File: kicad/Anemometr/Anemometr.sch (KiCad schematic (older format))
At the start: 154 parts, among them J1 Conn_01x01_Female, J10 Z3, J11 Z3, J12 Z4, J13 Z4, J14 SWD, J15 SWC, J16 Z4, J17 Z4, J18 1, J19 2, J2 Conn_01x01_Female, J20 3, J21 4, J22 5, J23 6, J24 7, J25 8, J26 Z4, J27 Z4, J28 Z4, J29 Z4, J3 RST, J30 Z4, J31 Z4, J32 Z4, J33 Z4, J34 Z4, J35 Z4, J4 TxD, J5 RxD, J6 Z1, J7 Z1, J8 Z2, J9 Z2, U1 TS5A3166DBVR, U10 MCP1700-3002E, U2 LMV7239, U3 TS5A3166DBVR, U4 TS5A3166DBVR, U5 STM32F103C8Tx, U6 TS5A3166DBVR, U7 LM2734Y, U8 MCP1700-5002E, U9 MCP1700-3002E, Y1 8MHz, Y2 25MHz

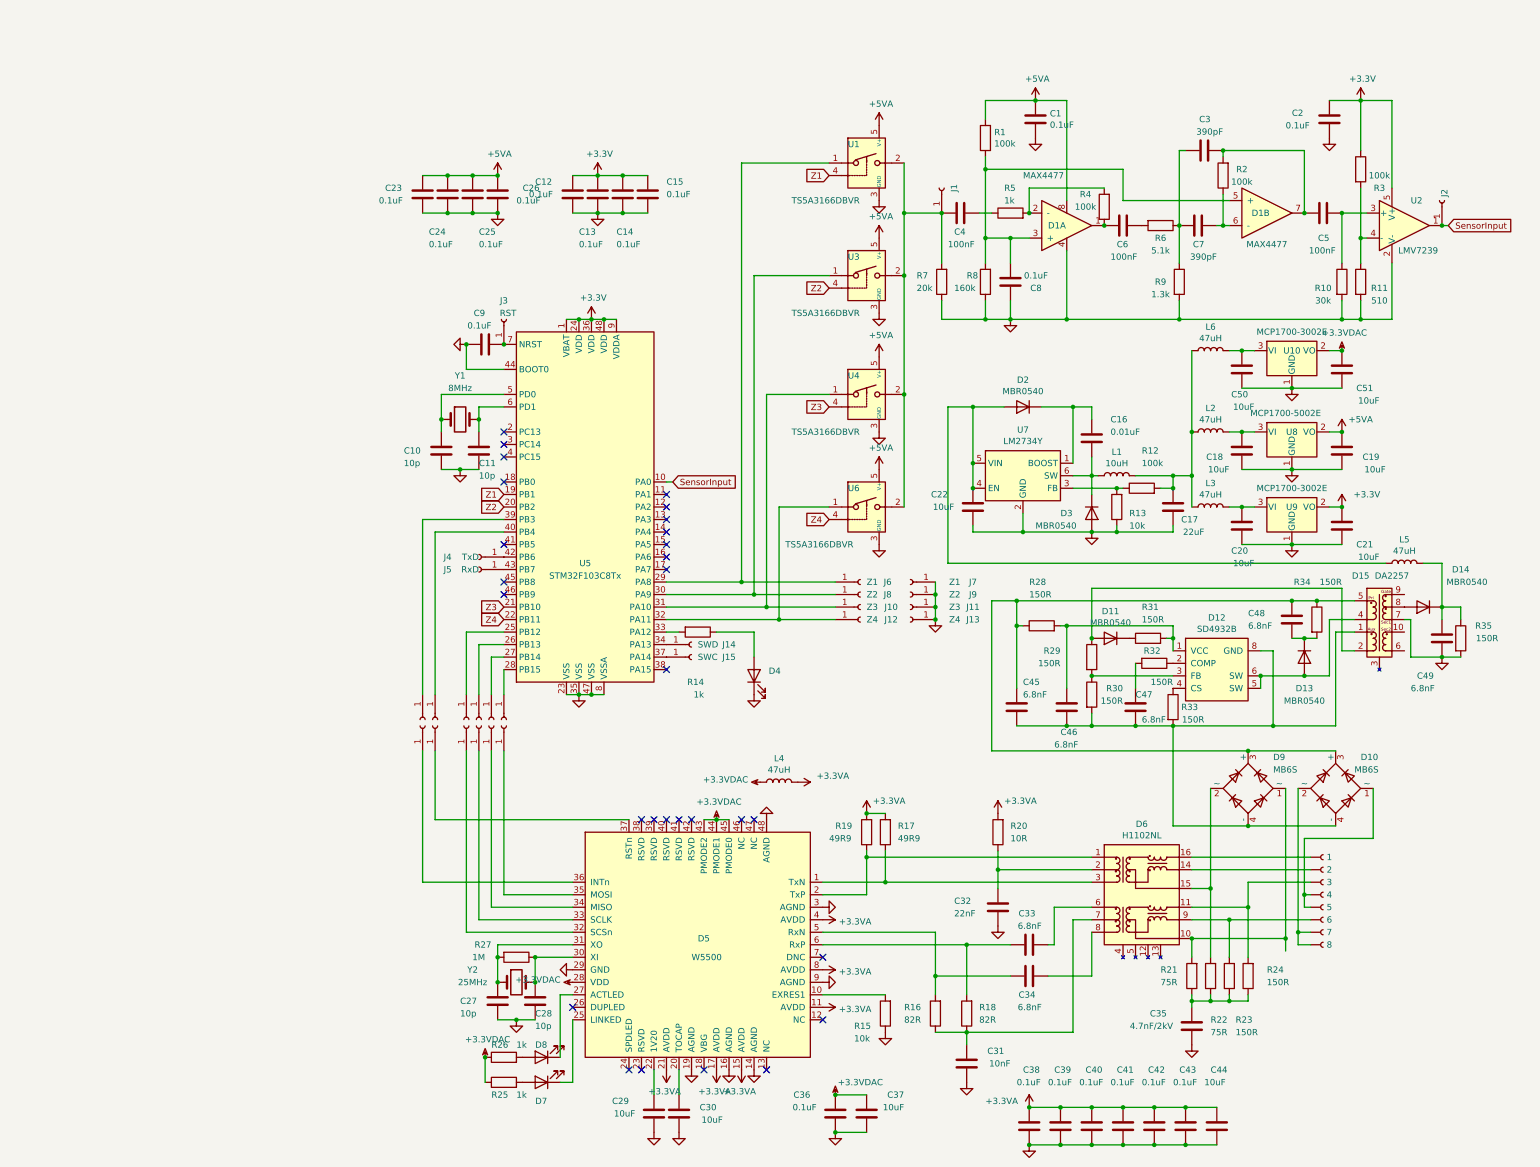
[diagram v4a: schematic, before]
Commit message: изменено:      kicad/Anemometr/Anemometr.kicad_pcb 	изменено:      kicad/Anemometr/Anemometr.kicad_pcb-bak 	изменено:      kicad/Anemometr/Anemometr.sch 	изменено:      kicad/Anemometr/Anemometr.sch-bak
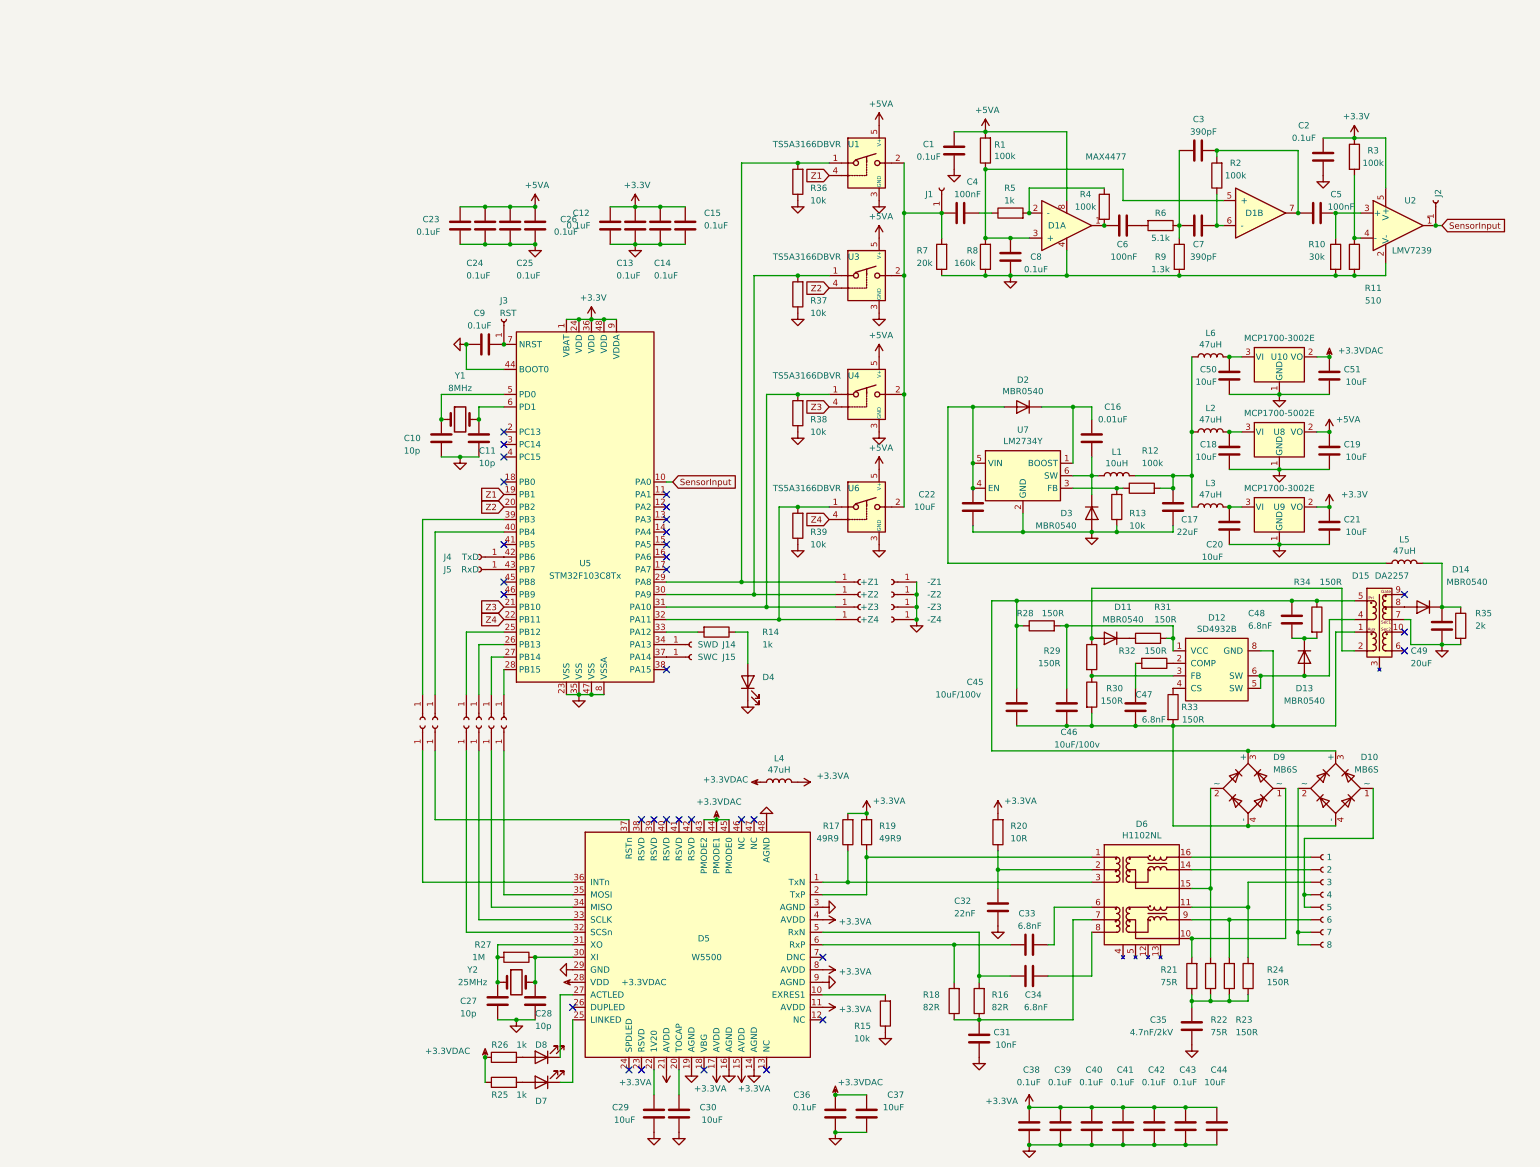
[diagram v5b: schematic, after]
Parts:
- added R36, R37, R38, R39: 10k, Resistor_SMD:R_0805_2012Metric, symbol Device:R
- C45, C46: value 6.8nF -> 10uF/100v
- C49: value 6.8nF -> 20uF
- J10: value Z3 -> +Z3
- J11: value Z3 -> -Z3
- J12: value Z4 -> +Z4
- J13: value Z4 -> -Z4
- J6: value Z1 -> +Z1
- J7: value Z1 -> -Z1
- J8: value Z2 -> +Z2
- J9: value Z2 -> -Z2
- R35: value 150R -> 2k
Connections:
- net GND: now also R36.1, R37.1, R38.1, R39.1
- net at J6.1 (Pin_1), U1.1, U5.29 (PA8): now also R36.2
- net at J8.1 (Pin_1), U3.1, U5.30 (PA9): now also R37.2
- net at J10.1 (Pin_1), U4.1, U5.31 (PA10): now also R38.2
- net at J12.1 (Pin_1), U5.32 (PA11), U6.1: now also R39.2
- no-connect marks 29 -> 32
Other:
- moved on the sheet: C1, C10, C11, C12, C13, C14, C15, C18, C19, C2, C20, C21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

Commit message: изменено:      kicad/Anemometr/Anemometr.sch 	изменено:      kicad/Anemometr/Anemometr.sch-bak 	изменено:      stm32cubeide/Anemometer/Anemometer.ioc 	изменено:      stm32cubeide/Anemometer/Core/Inc/main.h 	изменено:      stm32cubeide/Anemometer/Core/Src/main.c 	изменено:      stm32cubeide/Anemometer/Core/Src/stm32f1xx_it.c 	изменено:      stm32cubeide/Anemometer/Release/Anemometer.bin 	изменено:      stm32cubeide/Anemometer/Release/Anemometer.elf 	изменено:      stm32cubeide/Anemometer/Release/Anemometer.list 	изменено:      stm32cubeide/Anemometer/Release/Anemometer.map 	изменено:      stm32cubeide/Anemometer/Release/Core/Src/main.o 	изменено:      stm32cubeide/Anemometer/Release/Core/Src/main.su 	изменено:      stm32cubeide/Anemometer/Release/Core/Src/stm32f1xx_it.o 	изменено:      stm32cubeide/Anemometer/Release/Core/Src/stm32f1xx_it.su
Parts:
- C5: value 100nF -> 1.5nF
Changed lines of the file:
@@
 P 10950 2100
 F 0 "C5" V 11100 1900 50  0000 L CNN
-F 1 "100nF" V 11000 1800 50  0000 L CNN
+F 1 "1.5nF" V 11000 1800 50  0000 L CNN
 F 2 "Capacitor_SMD:C_0805_2012Metric" H 10988 1950 50  0001 C CNN
 F 3 "~" H 10950 2100 50  0001 C CNN

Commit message: изменено:      kicad/Anemometr/Anemometr.sch 	изменено:      kicad/Anemometr/Anemometr.sch-bak 	изменено:      stm32cubeide/Anemometer/Anemometer.ioc 	изменено:      stm32cubeide/Anemometer/Core/Inc/main.h 	изменено:      stm32cubeide/Anemometer/Core/Inc/stm32f1xx_it.h 	изменено:      stm32cubeide/Anemometer/Core/Src/main.c 	изменено:      stm32cubeide/Anemometer/Core/Src/stm32f1xx_hal_msp.c 	изменено:      stm32cubeide/Anemometer/Core/Src/stm32f1xx_it.c 	изменено:      stm32cubeide/Anemometer/Release/Anemometer.bin 	изменено:      stm32cubeide/Anemometer/Release/Anemometer.elf 	изменено:      stm32cubeide/Anemometer/Release/Anemometer.list 	изменено:      stm32cubeide/Anemometer/Release/Anemometer.map 	изменено:      stm32cubeide/Anemometer/Release/Core/Src/main.o 	изменено:      stm32cubeide/Anemometer/Release/Core/Src/main.su 	изменено:      stm32cubeide/Anemometer/Release/Core/Src/stm32f1xx_hal_msp.o 	изменено:      stm32cubeide/Anemometer/Release/Core/Src/stm32f1xx_hal_msp.su 	изменено:      stm32cubeide/Anemometer/Release/Core/Src/stm32f1xx_it.o 	изменено:      stm32cubeide/Anemometer/Release/Core/Src/stm32f1xx_it.su
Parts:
- R11: value 510 -> 3k
- R36, R37, R38, R39: value 10k -> 3k
- R4: value 100k -> 200k
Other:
- moved on the sheet: C2
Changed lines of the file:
@@
 P 9250 2050
 F 0 "R4" H 9400 1950 50  0000 C CNN
-F 1 "100k" H 9400 2050 50  0000 C CNN
+F 1 "200k" H 9400 2050 50  0000 C CNN
 F 2 "Resistor_SMD:R_0805_2012Metric" V 9180 2050 50  0001 C CNN
 F 3 "~" H 9250 2050 50  0001 C CNN
@@
 U 1 1 61CF8246
 P 8300 2450
-F 0 "R8" H 8450 2400 50  0000 R CNN
+F 0 "R8" H 8500 2400 50  0000 R CNN
 F 1 "160k" H 8550 2500 50  0000 R CNN
 F 2 "Resistor_SMD:R_0805_2012Metric" V 8230 2450 50  0001 C CNN
@@
 U 1 1 61CF86C2
 P 9850 2450
-F 0 "R9" H 9700 2450 50  0000 C CNN
-F 1 "1.3k" H 9700 2350 50  0000 C CNN
+F 0 "R9" H 9700 2500 50  0000 C CNN
+F 1 "1.3k" H 9700 2400 50  0000 C CNN
 F 2 "Resistor_SMD:R_0805_2012Metric" V 9780 2450 50  0001 C CNN
 F 3 "~" H 9850 2450 50  0001 C CNN
@@
 L Device:C C2
 U 1 1 61CFA6DA
-P 11000 1650
-F 0 "C2" H 10800 1900 50  0000 L CNN
-F 1 "0.1uF" H 10750 1800 50  0000 L CNN
-F 2 "Capacitor_SMD:C_0805_2012Metric" H 11038 1500 50  0001 C CNN
-F 3 "~" H 11000 1650 50  0001 C CNN
-	1    11000 1650
+P 11700 1650
+F 0 "C2" H 11850 1700 50  0000 L CNN
+F 1 "0.1uF" H 11850 1600 50  0000 L CNN
+F 2 "Capacitor_SMD:C_0805_2012Metric" H 11738 1500 50  0001 C CNN
+F 3 "~" H 11700 1650 50  0001 C CNN
+	1    11700 1650
 	1    0    0    -1
 $EndComp
@@
 L power:GND #PWR05
 U 1 1 61CFAC14
-P 11000 1800
-F 0 "#PWR05" H 11000 1550 50  0001 C CNN
-F 1 "GND" H 11005 1627 50  0001 C CNN
-F 2 "" H 11000 1800 50  0001 C CNN
-F 3 "" H 11000 1800 50  0001 C CNN
-	1    11000 1800
+P 11700 1800
+F 0 "#PWR05" H 11700 1550 50  0001 C CNN
+F 1 "GND" H 11705 1627 50  0001 C CNN
+F 2 "" H 11700 1800 50  0001 C CNN
+F 3 "" H 11700 1800 50  0001 C CNN
+	1    11700 1800
 	1    0    0    -1
 $EndComp
@@
 P 10150 1800
 F 0 "R2" H 10000 1700 50  0000 C CNN
-F 1 "100k" H 10000 1800 50  0000 C CNN
+F 1 "100k" H 9950 1800 50  0000 C CNN
 F 2 "Resistor_SMD:R_0805_2012Metric" V 10080 1800 50  0001 C CNN
 F 3 "~" H 10150 1800 50  0001 C CNN
@@
 U 1 1 61D69DFB
 P 10950 2100
-F 0 "C5" V 11100 1900 50  0000 L CNN
-F 1 "1.5nF" V 11000 1800 50  0000 L CNN
+F 0 "C5" V 11200 2050 50  0000 L CNN
+F 1 "1.5nF" V 11100 2000 50  0000 L CNN
 F 2 "Capacitor_SMD:C_0805_2012Metric" H 10988 1950 50  0001 C CNN
 F 3 "~" H 10950 2100 50  0001 C CNN
@@
 U 1 1 61D85B4A
 P 11600 2200
-F 0 "U2" H 11650 2400 50  0000 L CNN
+F 0 "U2" H 11550 2200 50  0000 L CNN
 F 1 "LMV7239" H 11550 2000 50  0000 L CNN
 F 2 "Package_TO_SOT_SMD:SOT-23-5" H 11600 1800 50  0001 C CNN
@@
 P 11250 2450
 F 0 "R11" H 11400 2200 50  0000 C CNN
-F 1 "510" H 11400 2100 50  0000 C CNN
+F 1 "3k" H 11400 2100 50  0000 C CNN
 F 2 "Resistor_SMD:R_0805_2012Metric" V 11180 2450 50  0001 C CNN
 F 3 "~" H 11250 2450 50  0001 C CNN
@@
 U 1 1 61E0D55F
 P 9400 2200
-F 0 "C6" V 9550 2150 50  0000 L CNN
-F 1 "100nF" V 9650 2100 50  0000 L CNN
+F 0 "C6" V 9150 2200 50  0000 L CNN
+F 1 "100nF" V 9250 2150 50  0000 L CNN
 F 2 "Capacitor_SMD:C_0805_2012Metric" H 9438 2050 50  0001 C CNN
 F 3 "~" H 9400 2200 50  0001 C CNN
@@
 U 1 1 61D49242
 P 11100 2450
-F 0 "R10" H 10950 2550 50  0000 C CNN
-F 1 "30k" H 10950 2450 50  0000 C CNN
+F 0 "R10" H 10950 2500 50  0000 C CNN
+F 1 "30k" H 10950 2400 50  0000 C CNN
 F 2 "Resistor_SMD:R_0805_2012Metric" V 11030 2450 50  0001 C CNN
 F 3 "~" H 11100 2450 50  0001 C CNN
@@
 P 9000 2200
 F 0 "D1" H 8800 2200 50  0000 L CNN
-F 1 "MAX4477" H 9100 2750 50  0000 L CNN
+F 1 "MAX4477" H 9000 2000 50  0000 L CNN
 F 2 "Package_SO:MSOP-8_3x3mm_P0.65mm" H 9000 2200 50  0001 C CNN
 F 3 "" H 9000 2200 50  0001 C CNN
@@
 	10150 1600 10800 1600
 Connection ~ 10150 1600
-Wire Wire Line
-	10200 2000 9400 2000
-Wire Wire Line
-	9400 1750 9400 2000
 Connection ~ 9850 2200
 Wire Wire Line
@@
 Connection ~ 8650 2100
 Wire Wire Line
-	9400 1750 8300 1750
-Wire Wire Line
-	8300 1750 8300 2300
+	8300 1750 8300 1800
 $Comp
 L MCU_ST_STM32F1:STM32F103C8Tx U5
@@
 U 1 1 61D8D3FA
 P 11250 1650
-F 0 "R3" H 11400 1700 50  0000 C CNN
-F 1 "100k" H 11400 1600 50  0000 C CNN
+F 0 "R3" H 11100 1700 50  0000 C CNN
+F 1 "100k" H 11100 1600 50  0000 C CNN
 F 2 "Resistor_SMD:R_0805_2012Metric" V 11180 1650 50  0001 C CNN
 F 3 "~" H 11250 1650 50  0001 C CNN
@@
 	11250 1800 11250 2300
 Wire Wire Line
-	11000 1500 11250 1500
-Wire Wire Line
 	11500 1500 11500 1900
 Connection ~ 11250 1500
@@
 	8050 7950 8500 7950
 Connection ~ 10150 2200
-Connection ~ 8300 1750
 Wire Wire Line
 	8950 1450 8950 2000
@@
 P 6800 4600
 F 0 "R39" H 6700 4650 50  0000 R CNN
-F 1 "10k" H 6700 4750 50  0000 R CNN
+F 1 "3k" H 6700 4750 50  0000 R CNN
 F 2 "Resistor_SMD:R_0805_2012Metric" V 6730 4600 50  0001 C CNN
 F 3 "~" H 6800 4600 50  0001 C CNN
@@
 P 6800 3700
 F 0 "R38" H 6700 3750 50  0000 R CNN
-F 1 "10k" H 6700 3850 50  0000 R CNN
+F 1 "3k" H 6700 3850 50  0000 R CNN
 F 2 "Resistor_SMD:R_0805_2012Metric" V 6730 3700 50  0001 C CNN
 F 3 "~" H 6800 3700 50  0001 C CNN
@@
 P 6800 2750
 F 0 "R37" H 6700 2800 50  0000 R CNN
-F 1 "10k" H 6700 2900 50  0000 R CNN
+F 1 "3k" H 6700 2900 50  0000 R CNN
 F 2 "Resistor_SMD:R_0805_2012Metric" V 6730 2750 50  0001 C CNN
 F 3 "~" H 6800 2750 50  0001 C CNN
@@
 P 6800 1850
 F 0 "R36" H 6700 1900 50  0000 R CNN
-F 1 "10k" H 6700 2000 50  0000 R CNN
+F 1 "3k" H 6700 2000 50  0000 R CNN
 F 2 "Resistor_SMD:R_0805_2012Metric" V 6730 1850 50  0001 C CNN
 F 3 "~" H 6800 1850 50  0001 C CNN
@@
 	1    0    0    -1
 $EndComp
+Wire Wire Line
+	11500 1500 11700 1500
+Connection ~ 11500 1500
+Wire Wire Line
+	9700 2000 10200 2000
+Wire Wire Line
+	8300 1800 9700 1800
+Connection ~ 8300 1800
+Wire Wire Line
+	8300 1800 8300 2300
+Wire Wire Line
+	9700 1800 9700 2000
 $EndSCHEMATC

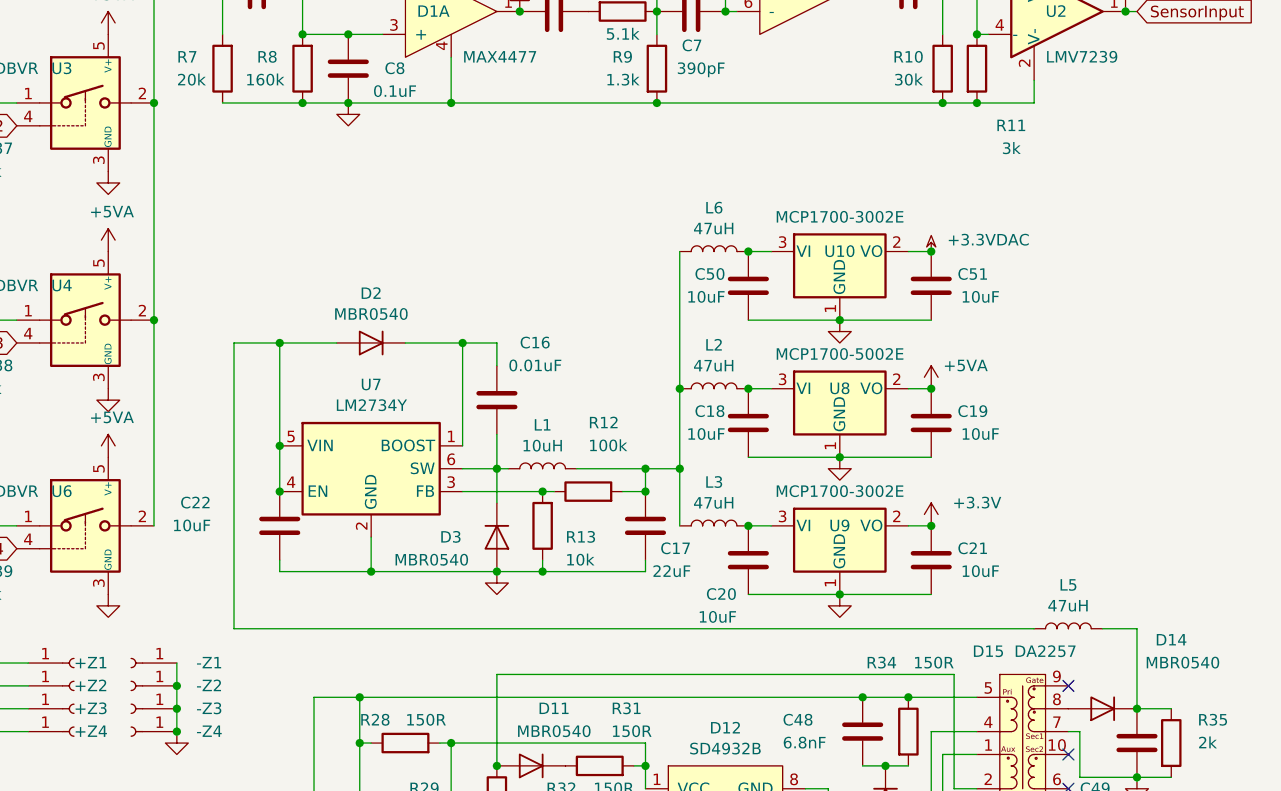
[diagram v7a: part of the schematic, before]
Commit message: изменено:      kicad/Anemometr/Anemometr.sch 	изменено:      kicad/Anemometr/Anemometr.sch-bak 	изменено:      stm32cubeide/Anemometer/Anemometer.ioc 	изменено:      stm32cubeide/Anemometer/Core/Inc/main.h 	изменено:      stm32cubeide/Anemometer/Core/Src/main.c 	изменено:      stm32cubeide/Anemometer/Core/Src/stm32f1xx_hal_msp.c 	изменено:      stm32cubeide/Anemometer/Core/Src/stm32f1xx_it.c 	изменено:      stm32cubeide/Anemometer/Release/Anemometer.bin 	изменено:      stm32cubeide/Anemometer/Release/Anemometer.elf 	изменено:      stm32cubeide/Anemometer/Release/Anemometer.list 	изменено:      stm32cubeide/Anemometer/Release/Anemometer.map 	изменено:      stm32cubeide/Anemometer/Release/Core/Src/main.o 	изменено:      stm32cubeide/Anemometer/Release/Core/Src/main.su 	изменено:      stm32cubeide/Anemometer/Release/Core/Src/stm32f1xx_hal_msp.o 	изменено:      stm32cubeide/Anemometer/Release/Core/Src/stm32f1xx_it.o 	изменено:      stm32cubeide/Anemometer/Release/Core/Src/stm32f1xx_it.su
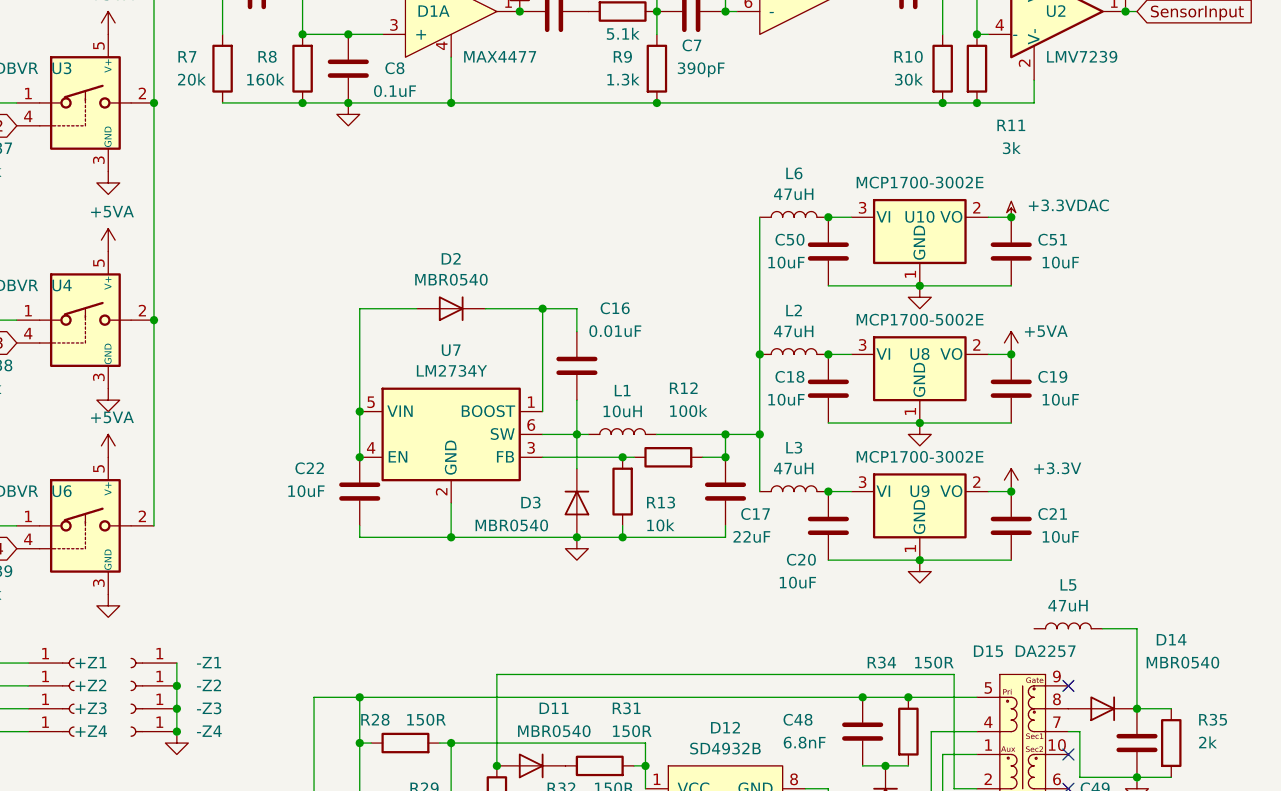
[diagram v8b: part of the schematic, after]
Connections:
- net at C22.2, D2.2 (A), U7.4 (EN)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: no longer L5.1
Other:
- moved on the sheet: C16, C17, C18, C19, C20, C21, C22, C50, C51, D2, D3, L1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
